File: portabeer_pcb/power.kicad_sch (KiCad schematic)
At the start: 32 parts, among them Q2 BSS84, U5 XC6206PxxxMR, U6 TPS54202DDC, U7 LTC2954-1

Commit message: electronics diagram and schematic
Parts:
- C20, C22, C27: footprint (none) -> Capacitor_THT:CP_Radial_D6.3mm_P2.50mm
- Q2: footprint Package_TO_SOT_SMD:SOT-323_SC-70 -> Package_TO_SOT_SMD:SOT-23
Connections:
- net GND: no longer U7. (GND)
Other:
- company: (none) -> ©2024 Luca Anastasio
- title: (none) -> Beerpak
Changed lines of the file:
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@@
 	(generator_version "8.0")
 	(paper "A4")
+	(title_block
+		(title "Beerpak")
+		(company "©2024 Luca Anastasio")
+	)
 	(junction
 		(at 114.3 69.85)
@@
 		)
 		(pin "2"
-		)
-		(pin ""
 		)
 		(pin "3"
@@
 			)
 		)
-		(property "Footprint" ""
+		(property "Footprint" "Capacitor_THT:CP_Radial_D6.3mm_P2.50mm"
 			(at 39.0652 64.77 0)
 			(effects
@@
 			)
 		)
-		(property "Footprint" "Package_TO_SOT_SMD:SOT-323_SC-70"
+		(property "Footprint" "Package_TO_SOT_SMD:SOT-23"
 			(at 222.885 72.39 0)
 			(effects
@@
 			)
 		)
-		(property "Footprint" ""
+		(property "Footprint" "Capacitor_THT:CP_Radial_D6.3mm_P2.50mm"
 			(at 55.5752 138.43 0)
 			(effects
@@
 			)
 		)
-		(property "Footprint" ""
+		(property "Footprint" "Capacitor_THT:CP_Radial_D6.3mm_P2.50mm"
 			(at 96.2152 138.43 0)
 			(effects

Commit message: added 3d models, started layout
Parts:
- L1: footprint Inductor_SMD:L_Taiyo-Yuden_NR-40xx -> portabeer:L_Taiyo-Yuden_NR-40xx
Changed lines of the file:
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@@
 			)
 		)
-		(property "Footprint" "Inductor_SMD:L_Taiyo-Yuden_NR-40xx"
+		(property "Footprint" "portabeer:L_Taiyo-Yuden_NR-40xx"
 			(at 107.95 57.15 0)
 			(effects

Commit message: partial routing
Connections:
- net +BATT: now also D2.2; no longer D2.1
- net VDC: now also D2.1; no longer D2.2

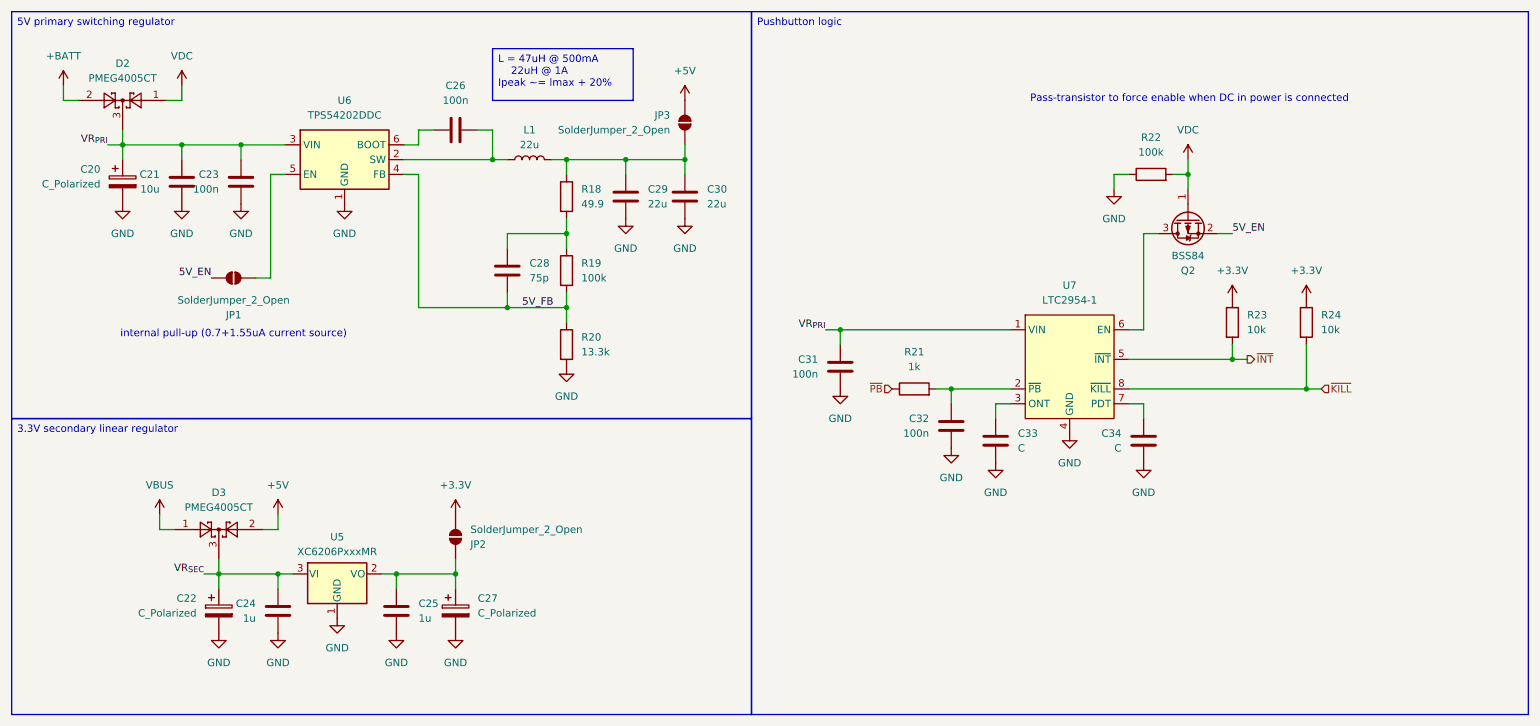
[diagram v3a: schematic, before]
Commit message: added capacitive sensor
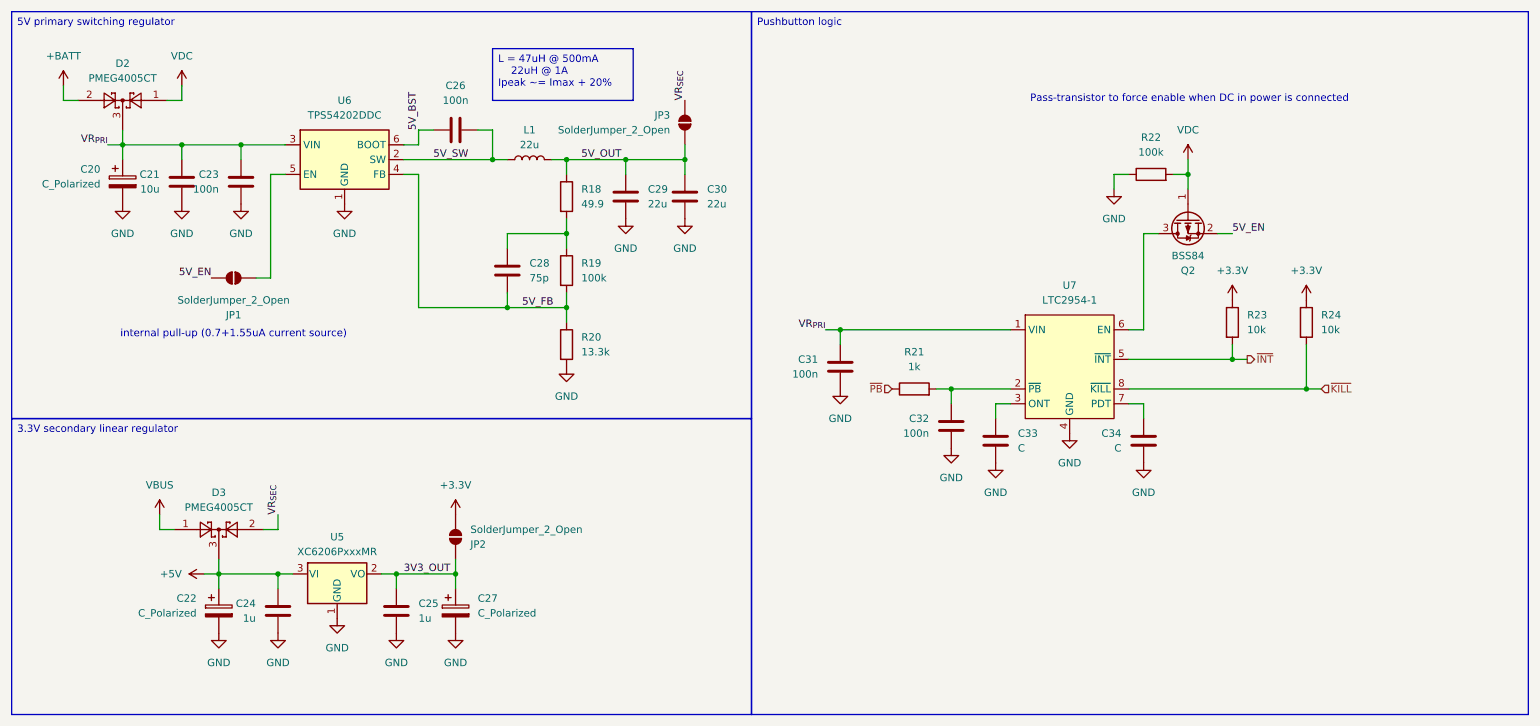
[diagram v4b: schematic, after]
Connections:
- net +5V: now also C22.1, C24.2, D3.3, U5.3 (VI); no longer D3.2, JP3.1 (A)
- net VR_{SEC}: now also D3.2, JP3.1 (A); no longer C22.1, C24.2, D3.3, U5.3 (VI)
- net 5V_SW: now reaches C26.1, L1.1, U6.2 (SW)
- net 5V_BST: now reaches C26.2, U6.6 (BOOT)
- net 5V_OUT: now reaches C29.1, C30.1, JP3.2 (B), L1.2, R18.1
- net 3V3_OUT: now reaches C25.1, C27.1, JP2.1 (A), U5.2 (VO)
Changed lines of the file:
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@@
 	)
 	(label "VR_{SEC}"
-		(at 52.07 128.27 180)
+		(at 64.77 118.11 90)
 		(effects
 			(font
 				(size 1.27 1.27)
 			)
-			(justify right bottom)
+			(justify left bottom)
+		)
+	)
+	(label "5V_OUT"
+		(at 116.84 57.15 0)
+		(effects
+			(font
+				(size 1.27 1.27)
+			)
+			(justify left bottom)
 		)
 	)
@@
 		)
 	)
+	(label "3V3_OUT"
+		(at 86.36 128.27 0)
+		(effects
+			(font
+				(size 1.27 1.27)
+			)
+			(justify left bottom)
+		)
+	)
+	(label "5V_BST"
+		(at 88.9 52.07 90)
+		(effects
+			(font
+				(size 1.27 1.27)
+			)
+			(justify left bottom)
+		)
+	)
 	(label "5V_EN"
 		(at 53.34 77.47 180)
@@
 		)
 	)
+	(label "5V_SW"
+		(at 91.44 57.15 0)
+		(effects
+			(font
+				(size 1.27 1.27)
+			)
+			(justify left bottom)
+		)
+	)
+	(label "VR_{SEC}"
+		(at 134.62 46.99 90)
+		(effects
+			(font
+				(size 1.27 1.27)
+			)
+			(justify left bottom)
+		)
+	)
 	(label "5V_FB"
 		(at 106.68 82.55 0)
@@
 	)
 	(symbol
-		(lib_id "power:+5V")
-		(at 134.62 46.99 0)
-		(unit 1)
-		(exclude_from_sim no)
-		(in_bom yes)
-		(on_board yes)
-		(dnp no)
-		(fields_autoplaced yes)
-		(property "Reference" "#PWR090"
-			(at 134.62 50.8 0)
-			(effects
-				(font
-					(size 1.27 1.27)
-				)
-				(hide yes)
-			)
-		)
-		(property "Value" "+5V"
-			(at 134.62 41.91 0)
-			(effects
-				(font
-					(size 1.27 1.27)
-				)
-			)
-		)
-		(property "Footprint" ""
-			(at 134.62 46.99 0)
-			(effects
-				(font
-					(size 1.27 1.27)
-				)
-				(hide yes)
-			)
-		)
-		(property "Datasheet" ""
-			(at 134.62 46.99 0)
-			(effects
-				(font
-					(size 1.27 1.27)
-				)
-				(hide yes)
-			)
-		)
-		(property "Description" "Power symbol creates a global label with name \"+5V\""
-			(at 134.62 46.99 0)
-			(effects
-				(font
-					(size 1.27 1.27)
-				)
-				(hide yes)
-			)
-		)
-		(pin "1"
-		)
-		(instances
-			(project ""
-				(path "/bb676e84-aa44-417a-9a70-748af1c322fb/1ca0c29a-6ba2-4ece-84f7-47eff36014c5"
-					(reference "#PWR090")
-					(unit 1)
-				)
-			)
-		)
-	)
-	(symbol
 		(lib_id "power:+3.3V")
 		(at 228.6 81.28 0)
@@
 	(symbol
 		(lib_id "power:+5V")
-		(at 64.77 118.11 0)
+		(at 52.07 128.27 90)
 		(unit 1)
 		(exclude_from_sim no)
@@
 		(fields_autoplaced yes)
 		(property "Reference" "#PWR081"
-			(at 64.77 121.92 0)
+			(at 55.88 128.27 0)
 			(effects
 				(font
@@
 		)
 		(property "Value" "+5V"
-			(at 64.77 113.03 0)
+			(at 48.26 128.2699 90)
 			(effects
 				(font
 					(size 1.27 1.27)
 				)
+				(justify left)
 			)
 		)
 		(property "Footprint" ""
-			(at 64.77 118.11 0)
+			(at 52.07 128.27 0)
 			(effects
 				(font
@@
 		)
 		(property "Datasheet" ""
-			(at 64.77 118.11 0)
+			(at 52.07 128.27 0)
 			(effects
 				(font
@@
 		)
 		(property "Description" "Power symbol creates a global label with name \"+5V\""
-			(at 64.77 118.11 0)
+			(at 52.07 128.27 0)
 			(effects
 				(font
